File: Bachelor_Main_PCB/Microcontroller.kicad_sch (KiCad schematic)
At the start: 34 parts, among them J3 M20-9990245, J4 M20-9990245, J5 M20-9990245, U3 STM32H7A3ZITxQ, U4 USB3320C-EZK-TR, Y1 SG-210STF 24Mhz

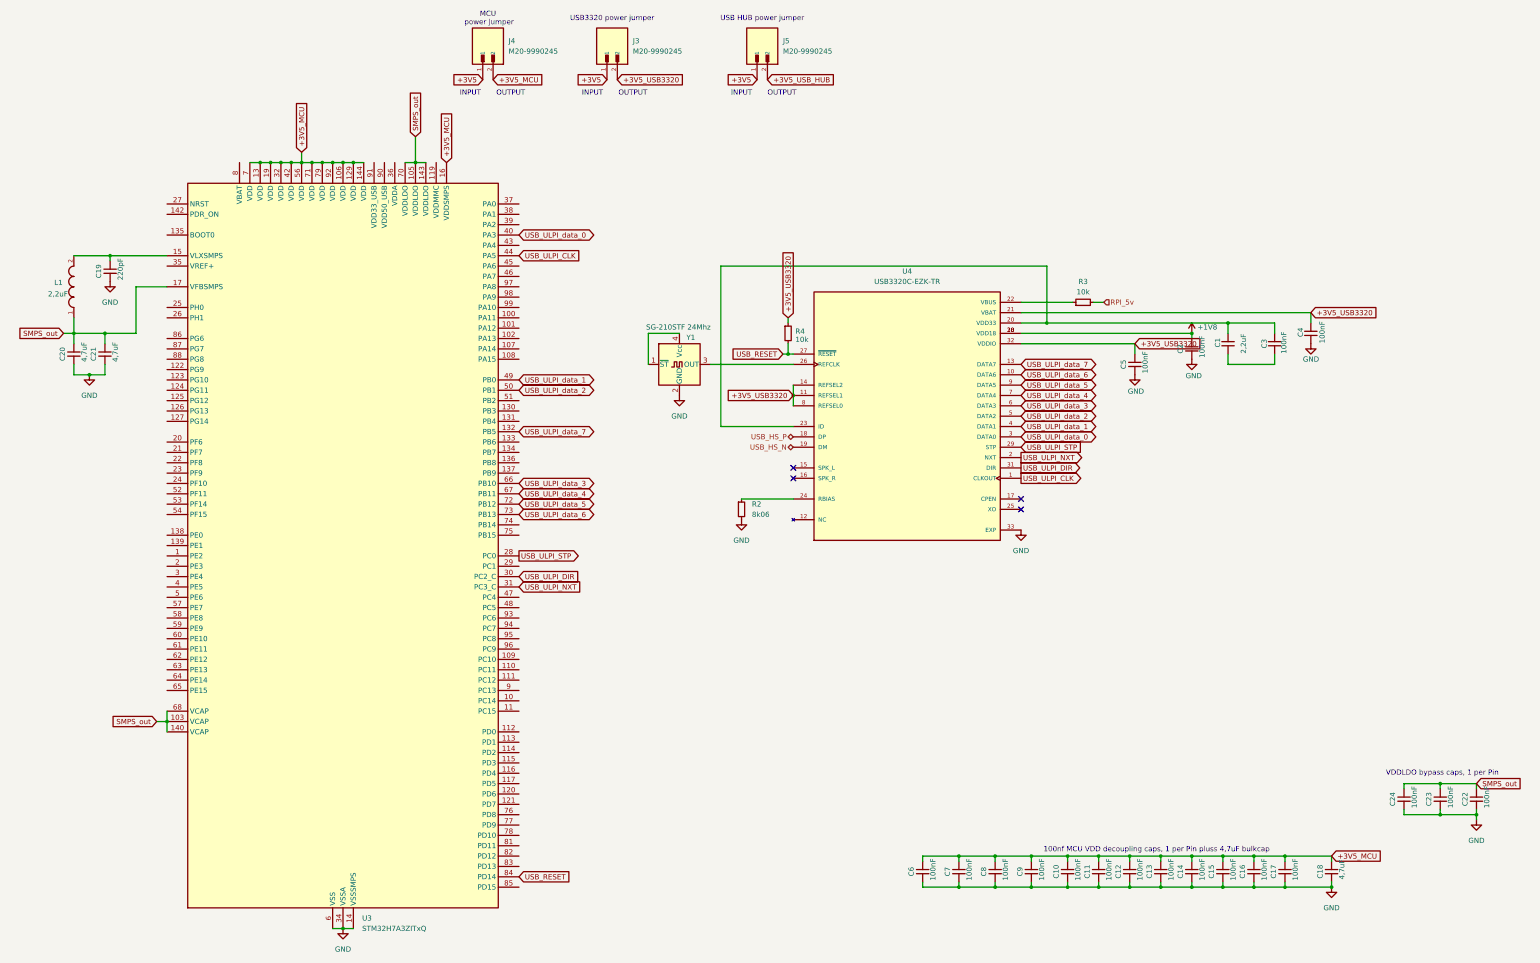
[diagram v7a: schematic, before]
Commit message: Add more bypass caps to MCU
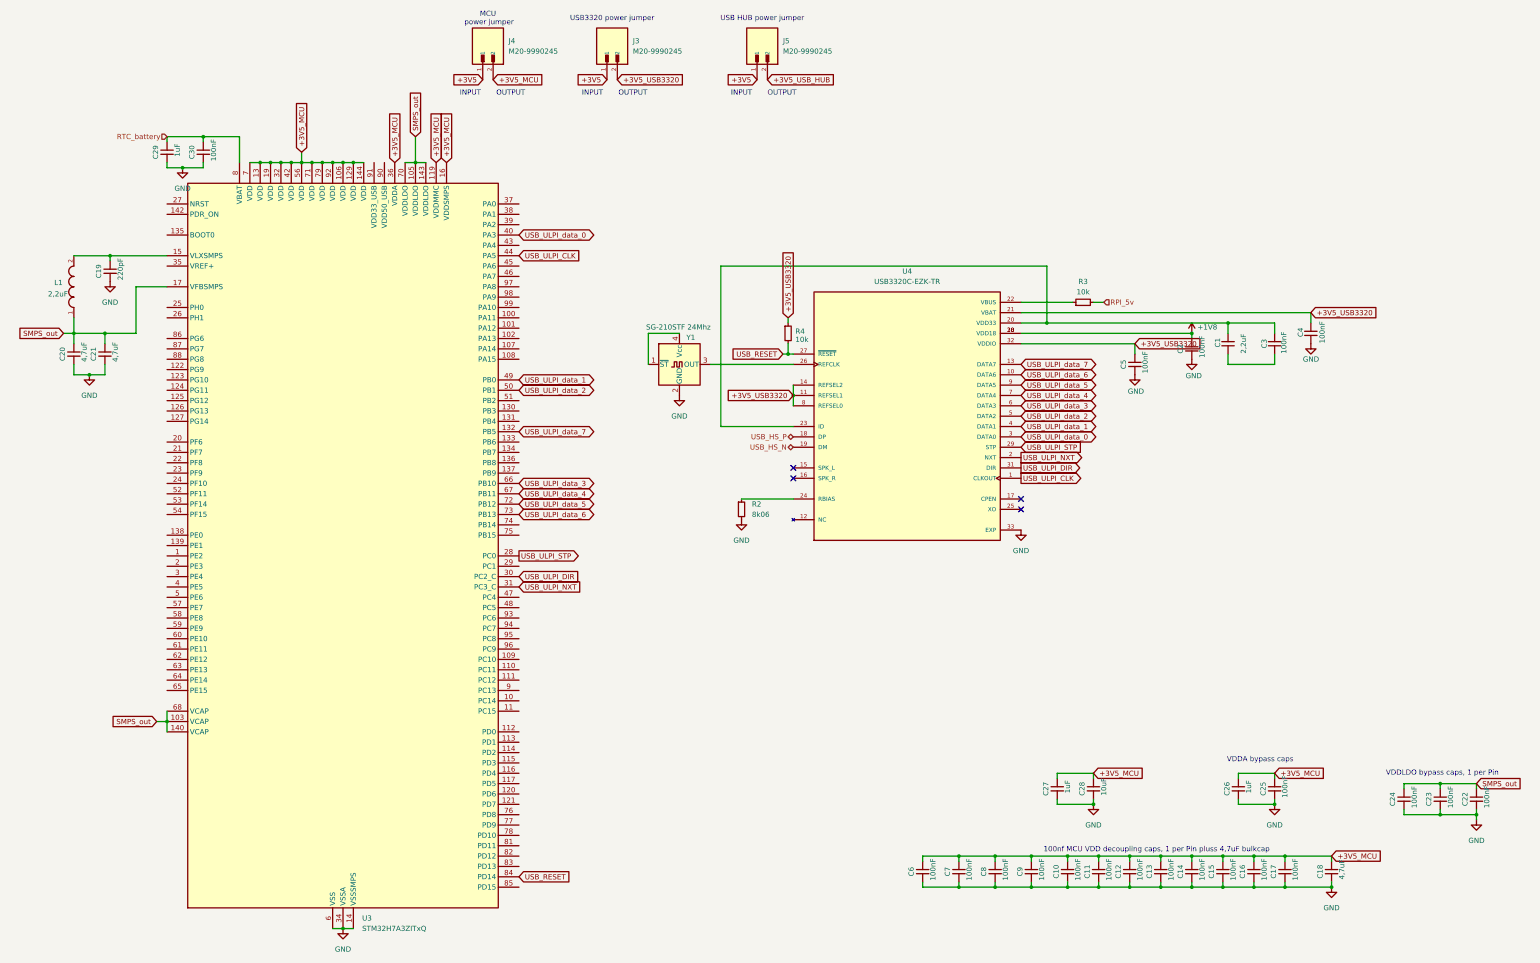
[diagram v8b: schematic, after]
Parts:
- added C25, C30: 100nF, Capacitor_SMD:C_0603_1608Metric, symbol Device:C_Small
- added C26, C27, C29: 1uF, Capacitor_SMD:C_0603_1608Metric, symbol Device:C_Small
- added C28: 10uF, Capacitor_SMD:C_0603_1608Metric, symbol Device:C_Small
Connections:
- net +3V5_MCU: now also U3.119 (VDDMMC), U3.36 (VDDA), C25.1, C26.1, C27.1, C28.1
- net GND: now also C25.2, C26.2, C27.2, C28.2, C29.2, C30.2
- net RTC_battery: now reaches U3.8 (VBAT)
- net RTC_battery: now also C29.1, C30.1
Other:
- note added: "VDDA bypass caps"
